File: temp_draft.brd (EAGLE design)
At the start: 100 x 80 mm, 37 parts, among them IC1 NCS21911SN2T1G, IC2 NCS21911SN2T1G, IC3 NCS21911SN2T1G, IC4 NCS21911SN2T1G

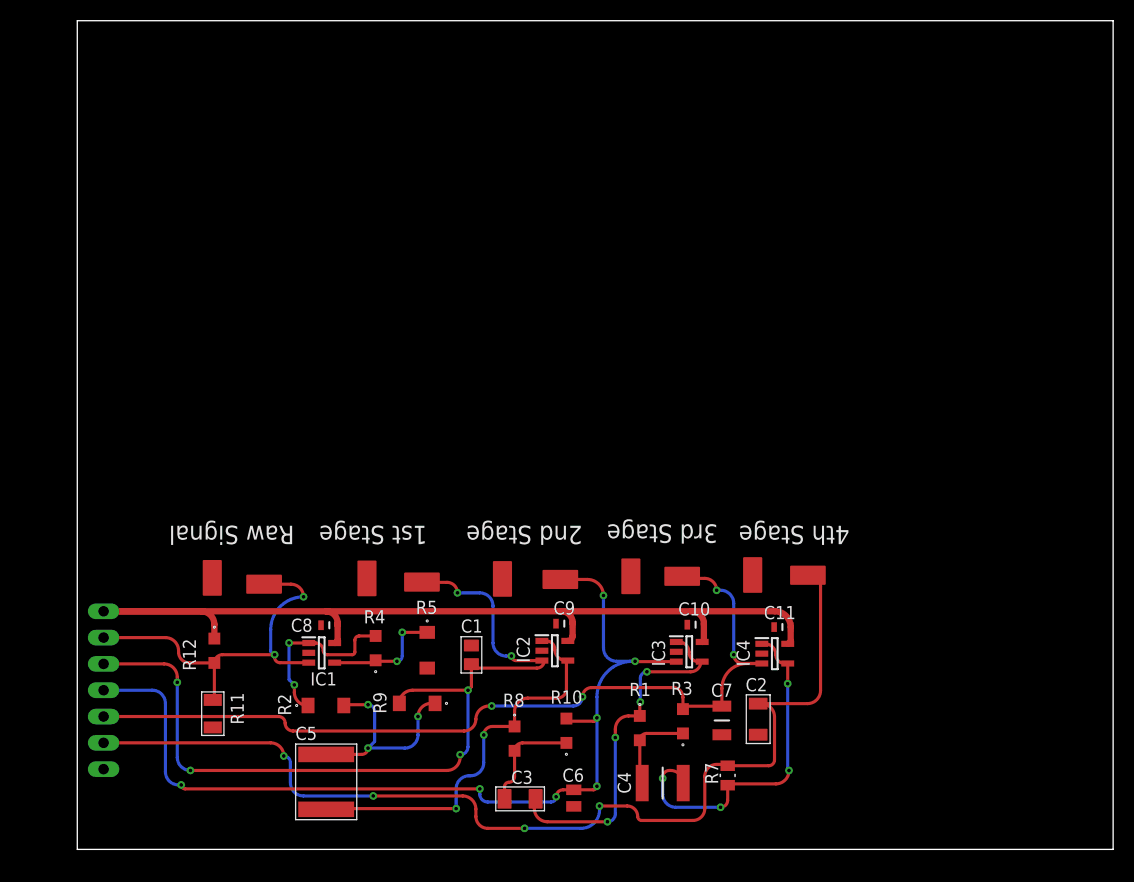
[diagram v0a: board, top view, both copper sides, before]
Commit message: added GND components for board
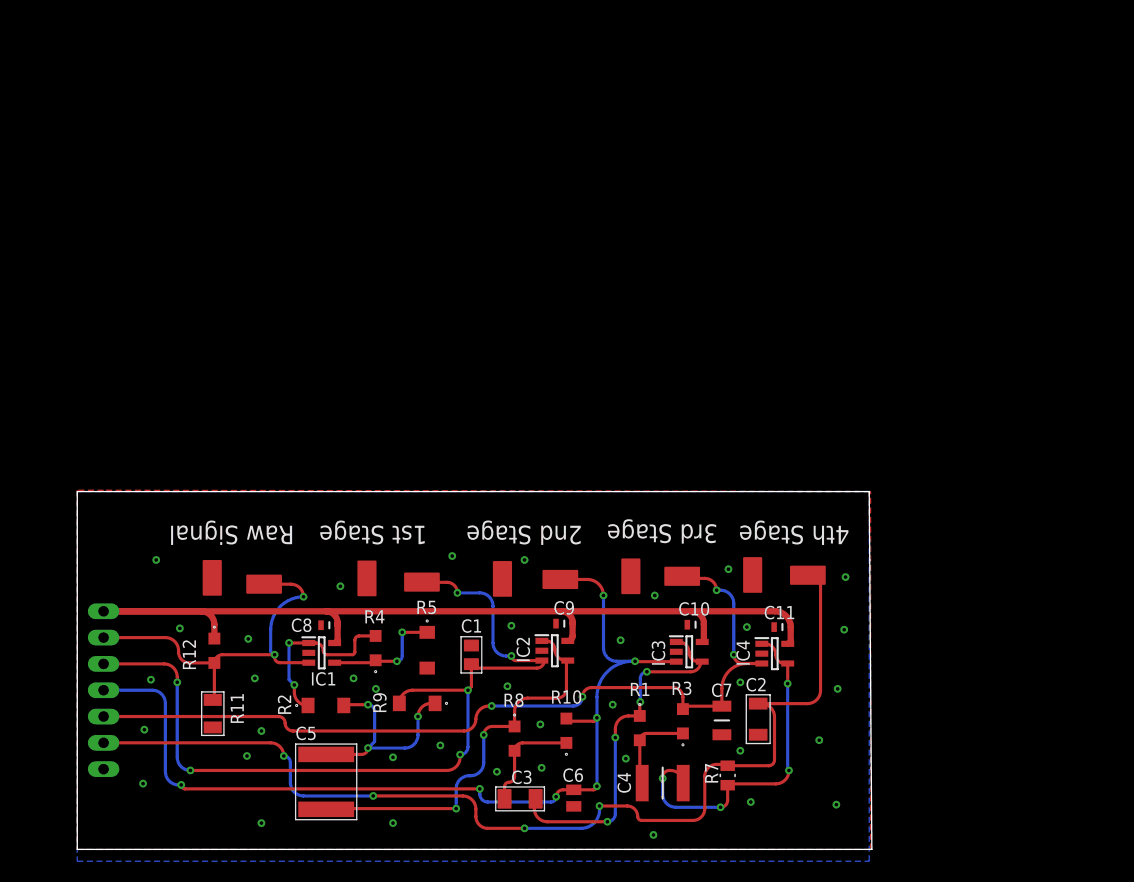
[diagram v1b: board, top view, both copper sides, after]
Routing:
- added copper zone on layer 1, net GND
- added copper zone on layer 16, net GND
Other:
- board size 100 x 80 mm -> 76.7 x 34.5 mm
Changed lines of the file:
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@@
 <board>
 <plain>
-<wire x1="0" y1="0" x2="100" y2="0" width="0" layer="20"/>
-<wire x1="100" y1="0" x2="100" y2="80" width="0" layer="20"/>
-<wire x1="100" y1="80" x2="0" y2="80" width="0" layer="20"/>
-<wire x1="0" y1="80" x2="0" y2="0" width="0" layer="20"/>
+<wire x1="0" y1="0" x2="76.708" y2="0" width="0" layer="20"/>
+<wire x1="76.708" y1="0" x2="76.454" y2="34.544" width="0" layer="20"/>
+<wire x1="76.454" y1="34.544" x2="0" y2="34.544" width="0" layer="20"/>
+<wire x1="0" y1="34.544" x2="0" y2="0" width="0" layer="20"/>
 <text x="48.768" y="31.242" size="1.778" layer="21" rot="SR180">2nd Stage</text>
 <text x="33.782" y="31.242" size="1.778" layer="21" rot="SR180">1st Stage</text>
@@
 <contactref element="TP10" pad="P$1"/>
 <contactref element="JP2" pad="7"/>
-<wire x1="65.2018" y1="26.4922" x2="67.272" y2="21.463" width="0" layer="19" extent="1-1"/>
-<wire x1="53.4416" y1="26.3652" x2="67.272" y2="21.463" width="0" layer="19" extent="1-1"/>
-<wire x1="66.0854" y1="18.8976" x2="67.272" y2="21.463" width="0" layer="19" extent="1-1"/>
-<wire x1="66.0854" y1="18.8976" x2="58.89" y2="21.6916" width="0" layer="19" extent="1-1"/>
-<wire x1="41.0464" y1="26.1112" x2="58.89" y2="21.6916" width="0" layer="19" extent="1-1"/>
-<wire x1="41.0464" y1="26.1112" x2="57.8304" y2="19.0754" width="0" layer="19" extent="1-1"/>
-<wire x1="46.2154" y1="21.7932" x2="57.8304" y2="19.0754" width="0" layer="19" extent="1-1"/>
-<wire x1="27.9654" y1="26.162" x2="46.2154" y2="21.7932" width="0" layer="19" extent="1-1"/>
-<wire x1="44.851" y1="19.177" x2="27.9654" y2="26.162" width="0" layer="19" extent="1-1"/>
-<wire x1="23.5332" y1="21.6408" x2="44.851" y2="19.177" width="0" layer="19" extent="1-1"/>
-<wire x1="38.0492" y1="19.6816" x2="23.5332" y2="21.6408" width="0" layer="19" extent="1-1"/>
-<wire x1="33.782" y1="17.5028" x2="38.0492" y2="19.6816" width="0" layer="19" extent="1-1"/>
-<wire x1="65.7352" y1="11.0716" x2="66.0854" y2="18.8976" width="0" layer="19" extent="1-1"/>
-<wire x1="62.23" y1="11.066" x2="65.7352" y2="11.0716" width="0" layer="19" extent="1-1"/>
-<wire x1="13.0302" y1="26.2128" x2="33.782" y2="17.5028" width="0" layer="19" extent="1-1"/>
-<wire x1="22.3466" y1="18.9738" x2="13.0302" y2="26.2128" width="0" layer="19" extent="1-1"/>
-<wire x1="13.081" y1="11.7772" x2="22.3466" y2="18.9738" width="0" layer="19" extent="1-1"/>
-<wire x1="2.54" y1="7.747" x2="13.081" y2="11.7772" width="0" layer="19" extent="1-1"/>
-<wire x1="47.9298" y1="4.153" x2="44.851" y2="19.177" width="0" layer="19" extent="1-1"/>
+<polygon width="0.3048" layer="1">
+<vertex x="0" y="34.671"/>
+<vertex x="0" y="0"/>
+<vertex x="76.581" y="0"/>
+<vertex x="76.581" y="34.544"/>
+<vertex x="2.54" y="34.671"/>
+<vertex x="2.54" y="34.671"/>
+</polygon>
+<polygon width="0.3048" layer="16">
+<vertex x="0" y="34.544"/>
+<vertex x="0" y="-1.143"/>
+<vertex x="76.454" y="-1.143"/>
+<vertex x="76.454" y="34.544"/>
+</polygon>
+<via x="7.62" y="27.94" extent="1-16" drill="0.35"/>
+<wire x1="23.5332" y1="21.6408" x2="27.9654" y2="26.162" width="0" layer="19" extent="1-1"/>
 </signal>
 <signal name="N$1">
@@
 <wire x1="26.797" y1="20.193" x2="27.21" y2="20.606" width="0.3048" layer="1" curve="-90"/>
 <wire x1="27.21" y1="20.606" x2="28.8036" y2="20.606" width="0.3048" layer="1"/>
-<wire x1="20.447" y1="19.939" x2="20.955" y2="15.875" width="0" layer="19"/>
-<wire x1="20.447" y1="19.939" x2="20.955" y2="15.875" width="0" layer="19"/>
 </signal>
 <signal name="N$6">
@@
 <wire x1="13.2334" y1="21.717" x2="13.2334" y2="20.352" width="0.6096" layer="1"/>
 </signal>
+<signal name="GND1">
+<via x="9.906" y="21.336" extent="1-16" drill="0.35"/>
+</signal>
+<signal name="GND2">
+<via x="6.35" y="6.35" extent="1-16" drill="0.35"/>
+</signal>
+<signal name="GND3">
+<via x="16.51" y="20.32" extent="1-16" drill="0.35"/>
+</signal>
+<signal name="GND4">
+<via x="17.78" y="11.43" extent="1-16" drill="0.35"/>
+</signal>
+<signal name="GND5">
+<via x="17.78" y="2.54" extent="1-16" drill="0.35"/>
+</signal>
+<signal name="GND6">
+<via x="25.4" y="25.4" extent="1-16" drill="0.35"/>
+</signal>
+<signal name="GND7">
+<via x="26.67" y="16.51" extent="1-16" drill="0.35"/>
+</signal>
+<signal name="GND8">
+<via x="30.48" y="8.89" extent="1-16" drill="0.35"/>
+</signal>
+<signal name="GND9">
+<via x="30.48" y="2.54" extent="1-16" drill="0.35"/>
+</signal>
+<signal name="GND10">
+<via x="43.18" y="27.94" extent="1-16" drill="0.35"/>
+</signal>
+<signal name="GND11">
+<via x="41.91" y="21.59" extent="1-16" drill="0.35"/>
+</signal>
+<signal name="GND12">
+<via x="41.529" y="15.748" extent="1-16" drill="0.35"/>
+</signal>
+<signal name="GND13">
+<via x="40.513" y="7.493" extent="1-16" drill="0.35"/>
+</signal>
+<signal name="GND14">
+<via x="52.451" y="20.193" extent="1-16" drill="0.35"/>
+</signal>
+<signal name="GND15">
+<via x="51.689" y="13.97" extent="1-16" drill="0.35"/>
+</signal>
+<signal name="GND16">
+<via x="52.959" y="8.763" extent="1-16" drill="0.35"/>
+</signal>
+<signal name="GND17">
+<via x="62.865" y="27.051" extent="1-16" drill="0.35"/>
+</signal>
+<signal name="GND18">
+<via x="64.643" y="21.463" extent="1-16" drill="0.35"/>
+</signal>
+<signal name="GND19">
+<via x="64.008" y="16.129" extent="1-16" drill="0.35"/>
+</signal>
+<signal name="GND20">
+<via x="65.024" y="4.572" extent="1-16" drill="0.35"/>
+</signal>
+<signal name="GND21">
+<via x="7.112" y="16.383" extent="1-16" drill="0.35"/>
+</signal>
+<signal name="GND22">
+<via x="64.008" y="9.525" extent="1-16" drill="0.35"/>
+</signal>
+<signal name="N$2">
+<via x="6.477" y="11.557" extent="1-16" drill="0.35"/>
+</signal>
+<signal name="N$3">
+<via x="17.145" y="16.51" extent="1-16" drill="0.35"/>
+</signal>
+<signal name="N$4">
+<via x="16.383" y="9.017" extent="1-16" drill="0.35"/>
+</signal>
+<signal name="N$8">
+<via x="28.829" y="15.494" extent="1-16" drill="0.35"/>
+</signal>
+<signal name="N$9">
+<via x="35.052" y="10.033" extent="1-16" drill="0.35"/>
+</signal>
+<signal name="N$10">
+<via x="44.831" y="7.874" extent="1-16" drill="0.35"/>
+</signal>
+<signal name="N$11">
+<via x="44.704" y="12.065" extent="1-16" drill="0.35"/>
+</signal>
+<signal name="N$12">
+<via x="55.753" y="24.511" extent="1-16" drill="0.35"/>
+</signal>
+<signal name="N$13">
+<via x="55.626" y="1.397" extent="1-16" drill="0.35"/>
+</signal>
+<signal name="N$14">
+<via x="74.168" y="26.289" extent="1-16" drill="0.35"/>
+</signal>
+<signal name="N$15">
+<via x="74.041" y="21.209" extent="1-16" drill="0.35"/>
+</signal>
+<signal name="N$16">
+<via x="73.406" y="15.494" extent="1-16" drill="0.35"/>
+</signal>
+<signal name="N$17">
+<via x="71.628" y="10.541" extent="1-16" drill="0.35"/>
+</signal>
+<signal name="N$18">
+<via x="73.279" y="4.318" extent="1-16" drill="0.35"/>
+</signal>
+<signal name="N$19">
+<via x="36.195" y="28.321" extent="1-16" drill="0.35"/>
+</signal>
 </signals>

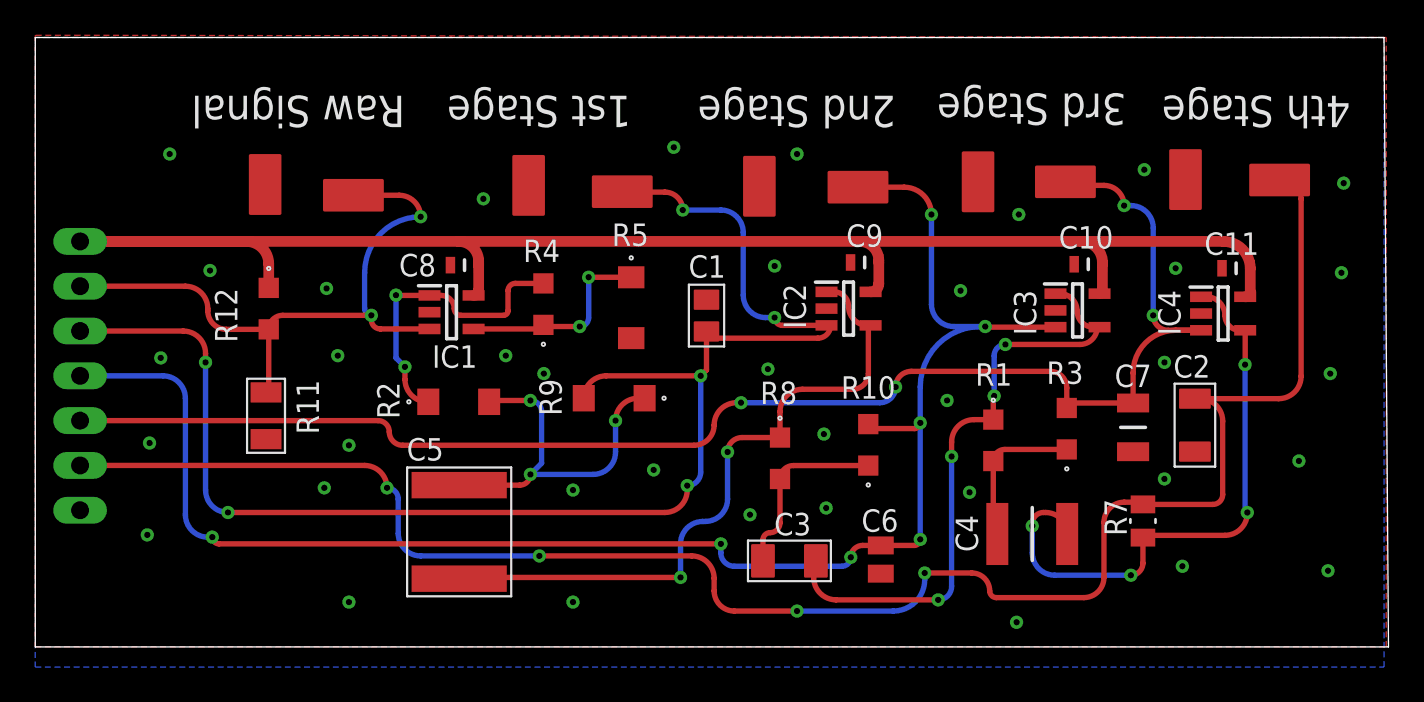
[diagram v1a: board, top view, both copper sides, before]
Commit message: with LED and tented Vias
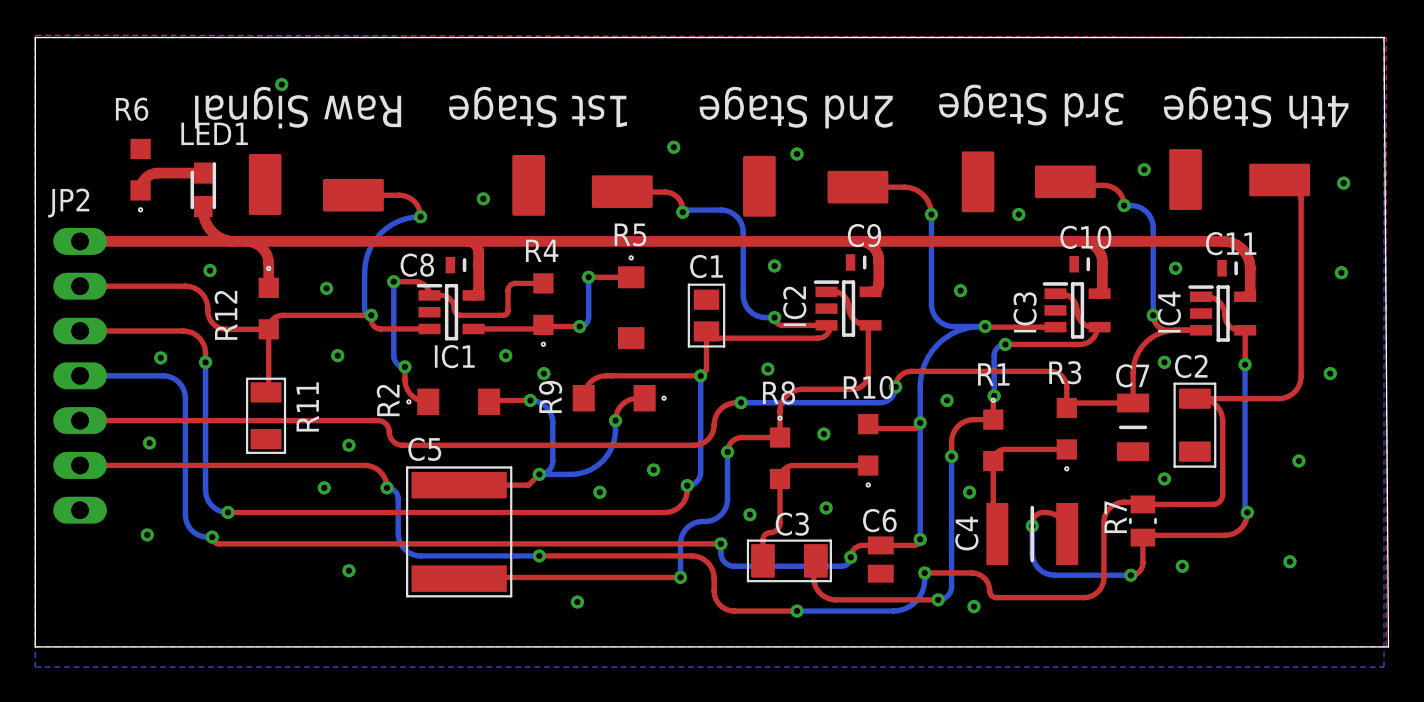
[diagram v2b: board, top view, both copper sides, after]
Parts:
- added LED1: 150080GS75000, SamacSys_Parts:LEDM2012X80N
- added R6: ERJ-P06J431V, SamacSys_Parts:ERJP06_(0805)
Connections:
- new net N$20: LED1.1, R6.1
- net GND: now also R6.2
- net V_12V: now also LED1.2
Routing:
- net V_12V: track 92.0 -> 85.5 mm
- net N$20: track 0.00 -> 3.96 mm
- net N$1: track 17.1 -> 18.3 mm
- net OUTPUT4: track 101.6 -> 101.0 mm
- net N$6: track 20.9 -> 20.3 mm
